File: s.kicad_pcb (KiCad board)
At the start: 2 copper layers, 200 x 75 mm, 89 parts, among them J2 UART connector, J4 Conn_01x02_Pin, J5 USB4105-GF-A, SW1 Z, SW10 D, SW11 S, SW12 K, SW13 W, SW14 R, SW15 STAR, SW16 R, SW17 B, SW18 G, SW19 S, SW2 T, SW20 Z, SW21 A, SW22 O, SW23 NUM, SW24 E, SW25 U, SW26 210-4MS, SW27 09.03290.01, SW3 P, SW4 H, SW5 STAR, SW6 F, SW7 P, SW8 L, SW9 T, U1 ESP32-S3-WROOM-1, U2 MCP1825S, U3 MCP1825S, U4 AP9101CK, U5 MCP73831-2-OT, U6 DMG6968U-7, U7 DMG6968U-7

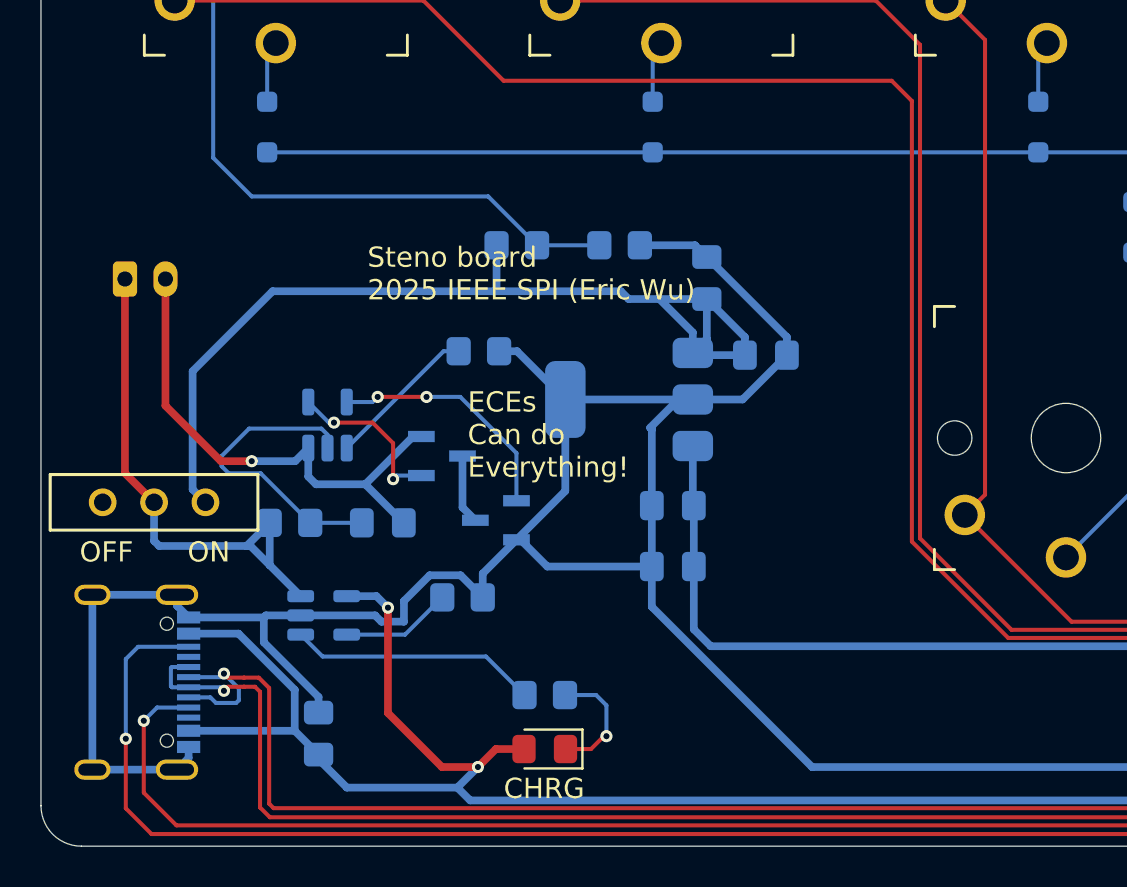
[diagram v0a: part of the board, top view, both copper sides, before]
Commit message: update silk screen to confrom to design rules
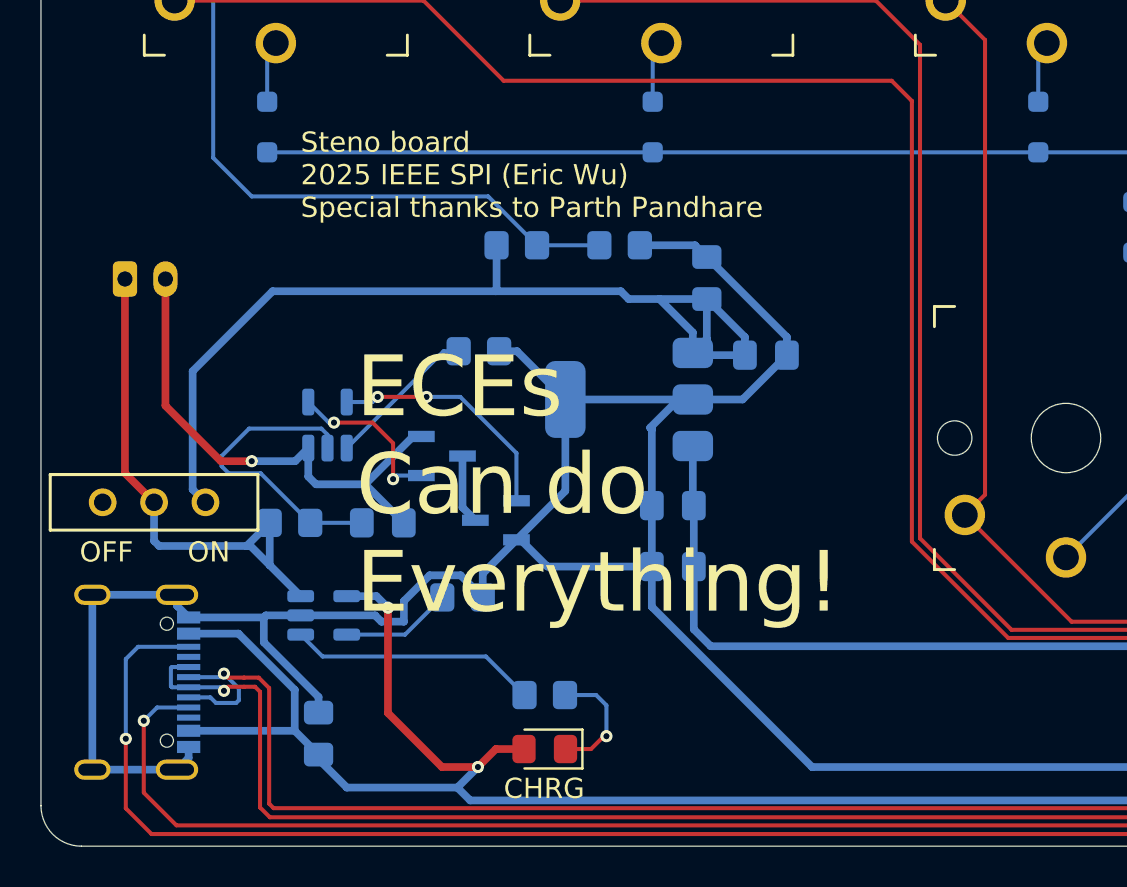
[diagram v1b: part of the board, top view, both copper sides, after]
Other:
- board text added: "Steno board 2025 IEEE SPI (Eric Wu) Special thanks to Parth Pandhare"
- board text removed: "Steno board 2025 IEEE SPI (Eric Wu)"

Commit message: reroute board
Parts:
- added R14: 0?, Resistor_SMD:R_0805_2012Metric_Pad1.20x1.40mm_HandSolder, B.Cu at (90.8, 130.7)
- added R15: 0?, Resistor_SMD:R_0805_2012Metric_Pad1.20x1.40mm_HandSolder, B.Cu at (95.0, 130.7)
- added R16: 0?, Resistor_SMD:R_0805_2012Metric_Pad1.20x1.40mm_HandSolder, B.Cu at (79.8, 124.1)
- added R17: 0?, Resistor_SMD:R_0805_2012Metric_Pad1.20x1.40mm_HandSolder, B.Cu at (76.8, 124.1)
- moved R10 15.2 mm to (61.5, 125.6), turned to -90 degrees
- moved U7 12.0 mm to (69.7, 111.0)
- moved U6 11.0 mm to (61.6, 113.0), turned to 90 degrees
- moved R11 5.84 mm to (217.3, 116.7)
- moved R4 5.84 mm to (217.3, 119.0)
- moved C9 4.35 mm to (88.0, 110.2)
- moved R8 4.35 mm to (76.8, 113.9)
- moved C10 4.35 mm to (91.0, 114.1)
- moved R12 4.35 mm to (78.7, 108.6)
- moved R13 4.35 mm to (83.7, 108.6)
- moved U3 4.35 mm to (84.2, 116.2)
- moved C11 4.33 mm to (68.1, 118.2)
- moved R7 4.33 mm to (63.5, 118.2)
- moved C8 4.21 mm to (86.2, 124.2)
- moved C7 4.21 mm to (86.2, 121.2)
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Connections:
- U1 pad 8: /CC1 -> Net-(U1-IO15)
- U1 pad 9: /CC2 -> Net-(U1-IO16)
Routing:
- net /CC2: track 204.6 -> 23.4 mm, vias 2 -> 0
- net Net-(U1-IO16): track 0.00 -> 160.7 mm, vias 0 -> 2
- net /CC1: track 196.3 -> 41.1 mm, vias 2 -> 0
- net Net-(U1-IO15): track 0.00 -> 144.5 mm
- net /battery_mgmt/vbatt_mon: track 262.7 -> 193.2 mm
- net /USB_D-: track 206.0 -> 182.6 mm, vias 2 -> 0
- net /USB_D+: track 205.9 -> 183.8 mm, vias 2 -> 0
- net /battery_mgmt/HV_CHR: track 48.7 -> 68.3 mm
- net Net-(D30-K): track 6.07 -> 18.7 mm
- net GND: track 359.6 -> 348.9 mm, vias 0 -> 3
- net Net-(U5-STAT): track 12.3 -> 3.01 mm
- net Net-(U4-DO): track 8.28 -> 2.34 mm, vias 2 -> 0
- net +3.3V: track 136.2 -> 131.4 mm
- net Net-(U4-CO): track 12.0 -> 7.23 mm
- net /battery_mgmt/between_mosfets: track 3.44 -> 7.68 mm
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- added copper zone on F.Cu, net GND

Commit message: add planes for ground
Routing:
- net GND: track 348.9 -> 7.79 mm, vias 3 -> 11
- added copper zone on B.Cu, net GND

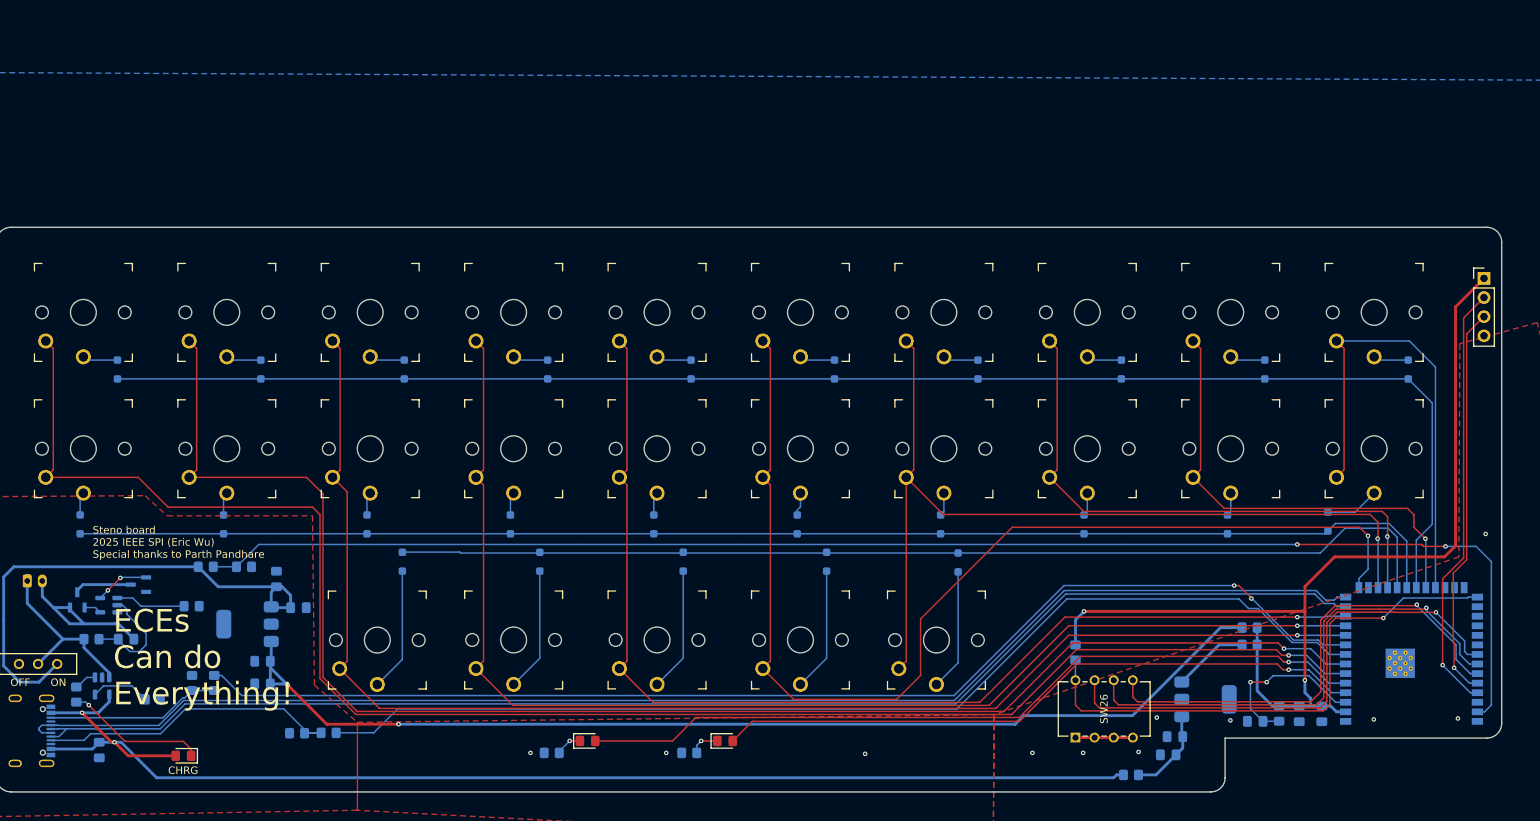
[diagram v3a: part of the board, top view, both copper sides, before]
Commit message: add 3 of 4 mounting holes
still need to think about the last one...
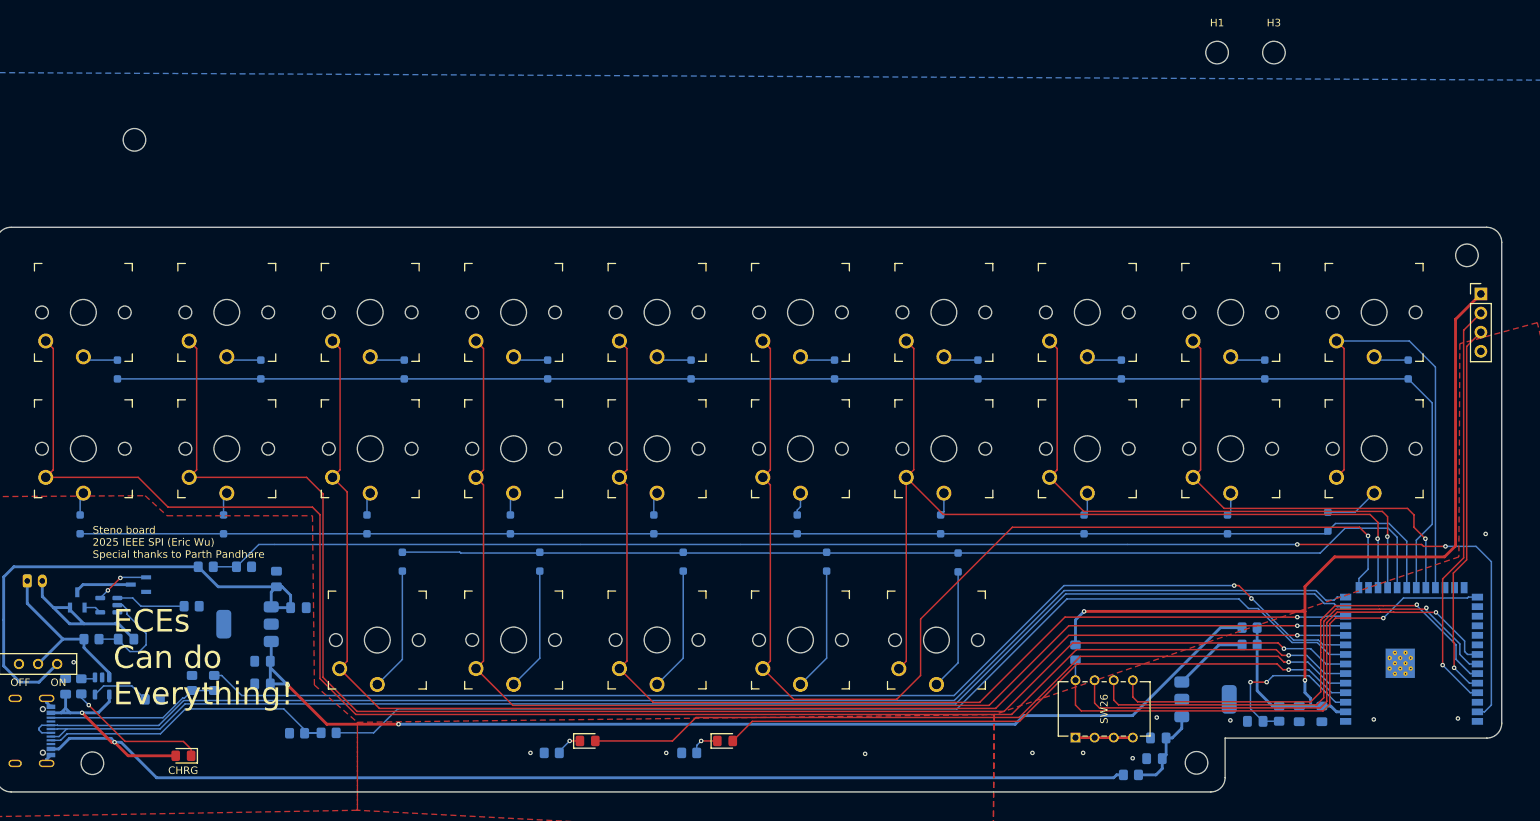
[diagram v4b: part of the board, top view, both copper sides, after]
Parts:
- added H1: MountingHole, MountingHole:MountingHole_3mm, F.Cu at (213.0, 40.3)
- added H2: MountingHole, MountingHole:MountingHole_3mm, F.Cu at (210.3, 134.7)
- added H3: MountingHole, MountingHole:MountingHole_3mm, F.Cu at (220.5, 40.3)
- added H4: MountingHole, MountingHole:MountingHole_3mm, F.Cu at (69.2, 51.9)
- added H5: MountingHole, MountingHole:MountingHole_3mm, F.Cu at (63.6, 134.7)
- added H6: MountingHole, MountingHole:MountingHole_3mm, F.Cu at (246.2, 67.3)
- moved C12 9.57 mm to (60.0, 124.5), turned to 90 degrees
- moved C2 2.22 mm to (205.2, 131.4)
- moved J2 2.10 mm to (248.0, 72.4)
- moved C4 1.90 mm to (204.7, 134.1)
- moved R10 1.28 mm to (62.1, 124.5)
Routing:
- net /VBUS: track 169.1 -> 173.1 mm
- net GND: track 7.79 -> 10.5 mm, vias 11 -> 12
- net /UART_TX: track 57.2 -> 55.0 mm
- net /UART_RX: track 52.3 -> 50.1 mm
- net +3.3V: track 131.4 -> 129.2 mm
- net Net-(U5-STAT): track 3.01 -> 1.90 mm

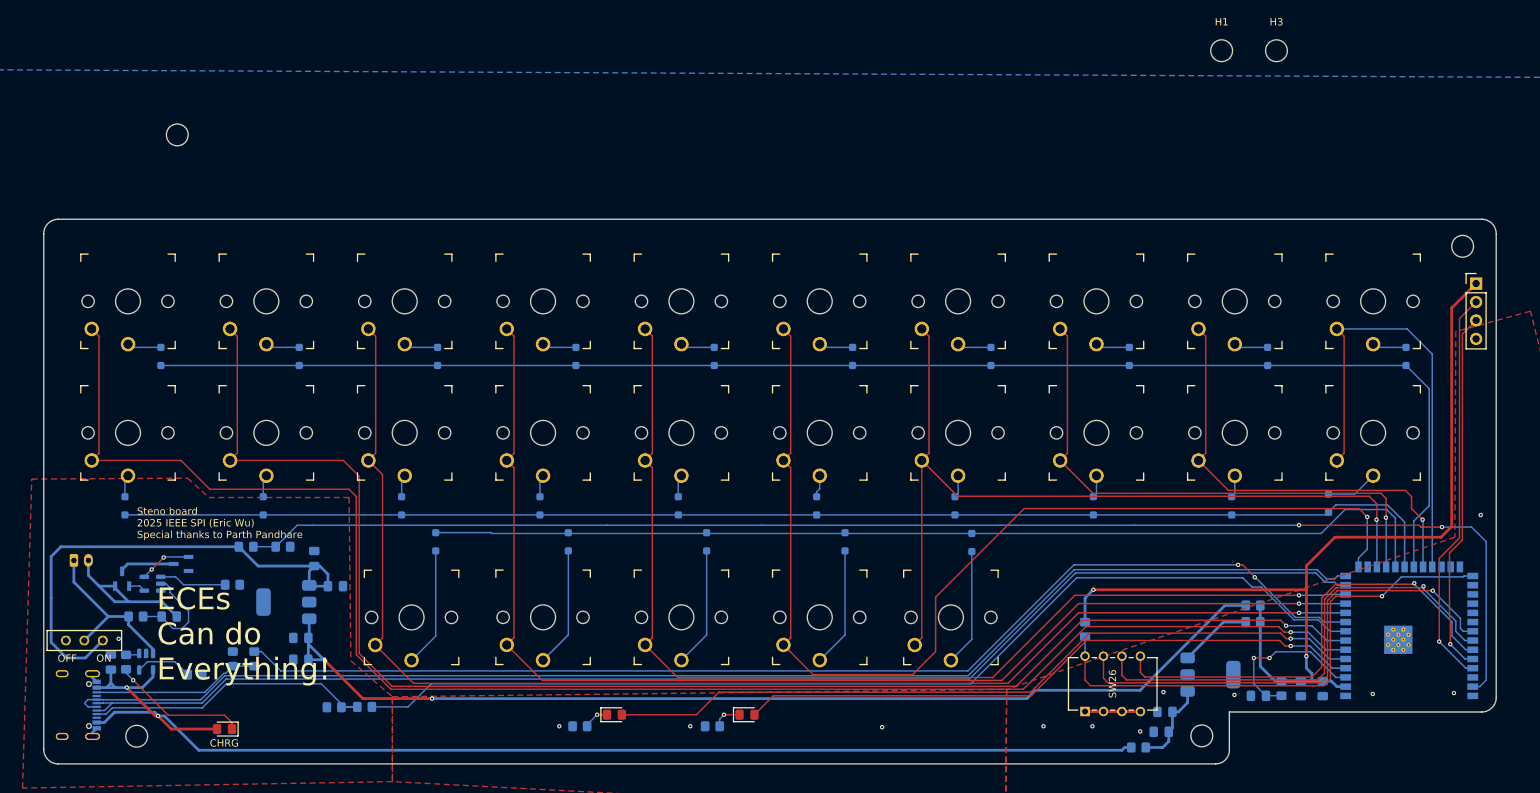
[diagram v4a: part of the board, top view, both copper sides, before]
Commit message: add the fourth mounting hole
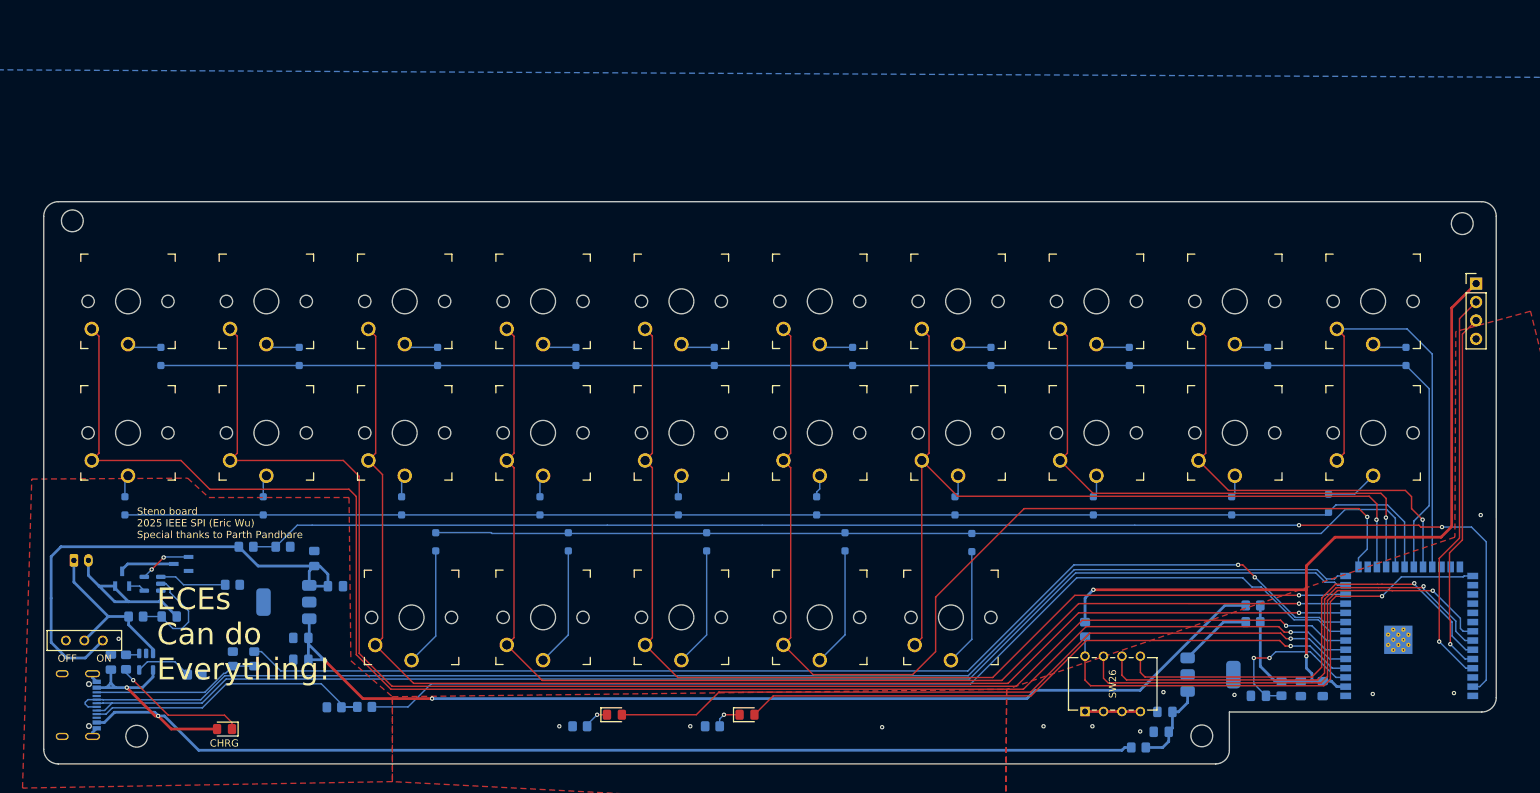
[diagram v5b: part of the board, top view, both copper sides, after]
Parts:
- removed H1, H3: MountingHole, MountingHole:MountingHole_3mm
- moved H4 18.7 mm to (54.7, 63.8)
- moved H6 3.12 mm to (246.1, 64.1)
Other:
- board size 200 x 75 mm -> 200 x 77.4 mm
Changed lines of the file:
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@@
 	(footprint "MountingHole:MountingHole_3mm"
 		(layer "F.Cu")
-		(at 246.1768 67.2592)
+		(at 246.126 64.135)
 		(descr "Mounting Hole 3mm, no annular, generated by kicad-footprint-generator mountinghole.py")
 		(tags "mountinghole")
@@
 	(footprint "MountingHole:MountingHole_3mm"
 		(layer "F.Cu")
-		(at 69.1896 51.9176)
+		(at 54.737 63.754)
 		(descr "Mounting Hole 3mm, no annular, generated by kicad-footprint-generator mountinghole.py")
 		(tags "mountinghole")
@@
 		(embedded_fonts no)
 	)
-	(footprint "MountingHole:MountingHole_3mm"
-		(layer "F.Cu")
-		(at 212.992 40.329)
-		(descr "Mounting Hole 3mm, no annular, generated by kicad-footprint-generator mountinghole.py")
-		(tags "mountinghole")
-		(property "Reference" "H1"
-			(at 0 -3.95 0)
-			(layer "F.SilkS")
-			(effects
-				(font
-					(size 1 1)
-					(thickness 0.15)
-				)
-			)
-		)
-		(property "Value" "MountingHole"
-			(at 0 3.95 0)
-			(layer "F.Fab")
-			(effects
-				(font
-					(size 1 1)
-					(thickness 0.15)
-				)
-			)
-		)
-		(property "Datasheet" "~"
-			(at 0 0 0)
-			(layer "F.Fab")
-			(hide yes)
-			(effects
-				(font
-					(size 1.27 1.27)
-					(thickness 0.15)
-				)
-			)
-		)
-		(property "Description" "Mounting Hole without connection"
-			(at 0 0 0)
-			(layer "F.Fab")
-			(hide yes)
-			(effects
-				(font
-					(size 1.27 1.27)
-					(thickness 0.15)
-				)
-			)
-		)
-		(property ki_fp_filters "MountingHole*")
-		(sheetname "/")
-		(sheetfile "s.kicad_sch")
-		(attr exclude_from_pos_files exclude_from_bom)
-		(fp_circle
-			(center 0 0)
-			(end 3 0)
-			(stroke
-				(width 0.15)
-				(type solid)
-			)
-			(fill no)
-			(layer "Cmts.User")
-		)
-		(fp_circle
-			(center 0 0)
-			(end 3.25 0)
-			(stroke
-				(width 0.05)
-				(type solid)
-			)
-			(fill no)
-			(layer "F.CrtYd")
-		)
-		(fp_text user "${REFERENCE}"
-			(at 0 0 0)
-			(layer "F.Fab")
-			(effects
-				(font
-					(size 1 1)
-					(thickness 0.15)
-				)
-			)
-		)
-		(pad "" np_thru_hole circle
-			(at 0 0)
-			(size 3 3)
-			(drill 3)
-			(layers "*.Cu" "*.Mask")
-		)
-		(embedded_fonts no)
-	)
-	(footprint "MountingHole:MountingHole_3mm"
-		(layer "F.Cu")
-		(at 220.542 40.329)
-		(descr "Mounting Hole 3mm, no annular, generated by kicad-footprint-generator mountinghole.py")
-		(tags "mountinghole")
-		(property "Reference" "H3"
-			(at 0 -3.95 0)
-			(layer "F.SilkS")
-			(effects
-				(font
-					(size 1 1)
-					(thickness 0.15)
-				)
-			)
-		)
-		(property "Value" "MountingHole"
-			(at 0 3.95 0)
-			(layer "F.Fab")
-			(effects
-				(font
-					(size 1 1)
-					(thickness 0.15)
-				)
-			)
-		)
-		(property "Datasheet" "~"
-			(at 0 0 0)
-			(layer "F.Fab")
-			(hide yes)
-			(effects
-				(font
-					(size 1.27 1.27)
-					(thickness 0.15)
-				)
-			)
-		)
-		(property "Description" "Mounting Hole without connection"
-			(at 0 0 0)
-			(layer "F.Fab")
-			(hide yes)
-			(effects
-				(font
-					(size 1.27 1.27)
-					(thickness 0.15)
-				)
-			)
-		)
-		(property ki_fp_filters "MountingHole*")
-		(sheetname "/")
-		(sheetfile "s.kicad_sch")
-		(attr exclude_from_pos_files exclude_from_bom)
-		(fp_circle
-			(center 0 0)
-			(end 3 0)
-			(stroke
-				(width 0.15)
-				(type solid)
-			)
-			(fill no)
-			(layer "Cmts.User")
-		)
-		(fp_circle
-			(center 0 0)
-			(end 3.25 0)
-			(stroke
-				(width 0.05)
-				(type solid)
-			)
-			(fill no)
-			(layer "F.CrtYd")
-		)
-		(fp_text user "${REFERENCE}"
-			(at 0 0 0)
-			(layer "F.Fab")
-			(effects
-				(font
-					(size 1 1)
-					(thickness 0.15)
-				)
-			)
-		)
-		(pad "" np_thru_hole circle
-			(at 0 0)
-			(size 3 3)
-			(drill 3)
-			(layers "*.Cu" "*.Mask")
-		)
-		(embedded_fonts no)
-	)
 	(footprint "key-switches:SW_Kailh_Choc_V1_THT"
 		(layer "F.Cu")
@@
 	)
 	(gr_line
-		(start 250.8 65.532)
-		(end 250.8 129.4)
+		(start 250.804419 129.4)
+		(end 250.8 63.11875)
 		(stroke
 			(width 0.05)
@@
 	)
 	(gr_line
-		(start 52.8 63.532)
-		(end 248.8 63.532)
+		(start 52.8 61.11875)
+		(end 248.8 61.11875)
 		(stroke
 			(width 0.05)
@@
 	)
 	(gr_arc
-		(start 50.8 65.532)
-		(mid 51.385786 64.117786)
-		(end 52.8 63.532)
+		(start 50.8 63.11875)
+		(mid 51.385786 61.704536)
+		(end 52.8 61.11875)
 		(stroke
 			(width 0.05)
@@
 		(layer "Edge.Cuts")
 	)
-	(gr_line
-		(start 50.8 136.532)
-		(end 50.8 65.532)
+	(gr_arc
+		(start 248.8 61.11875)
+		(mid 250.214214 61.704536)
+		(end 250.8 63.11875)
 		(stroke
 			(width 0.05)
@@
 		(layer "Edge.Cuts")
 	)
-	(gr_arc
-		(start 248.8 63.532)
-		(mid 250.214214 64.117786)
-		(end 250.8 65.532)
+	(gr_line
+		(start 50.8 63.11875)
+		(end 50.8 136.532)
 		(stroke
 			(width 0.05)
